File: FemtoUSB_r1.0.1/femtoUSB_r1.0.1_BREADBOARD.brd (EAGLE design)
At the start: 40.6 x 20.3 mm, 32 parts, among them IC1 ATSAMD21E18A-MUT

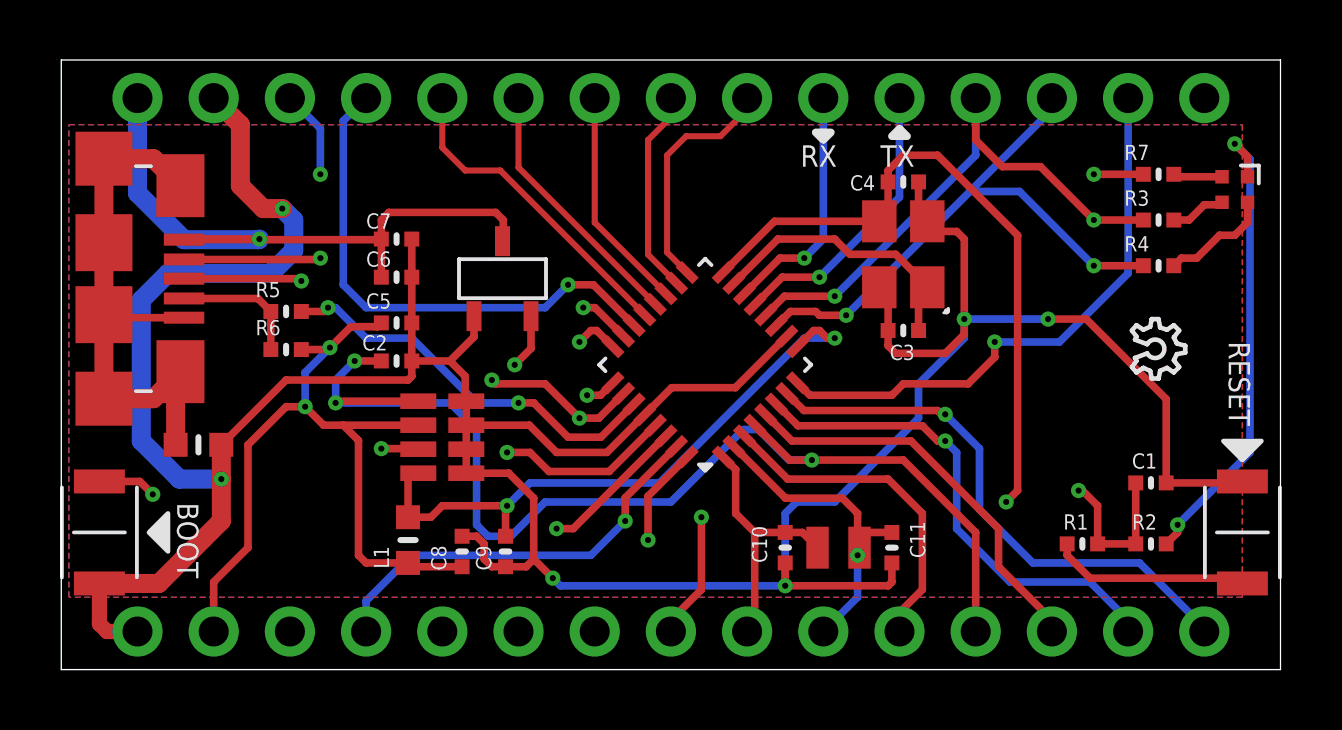
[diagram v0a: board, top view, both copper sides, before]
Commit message: Updating FemtoUSB r1.0.1 breadboard version
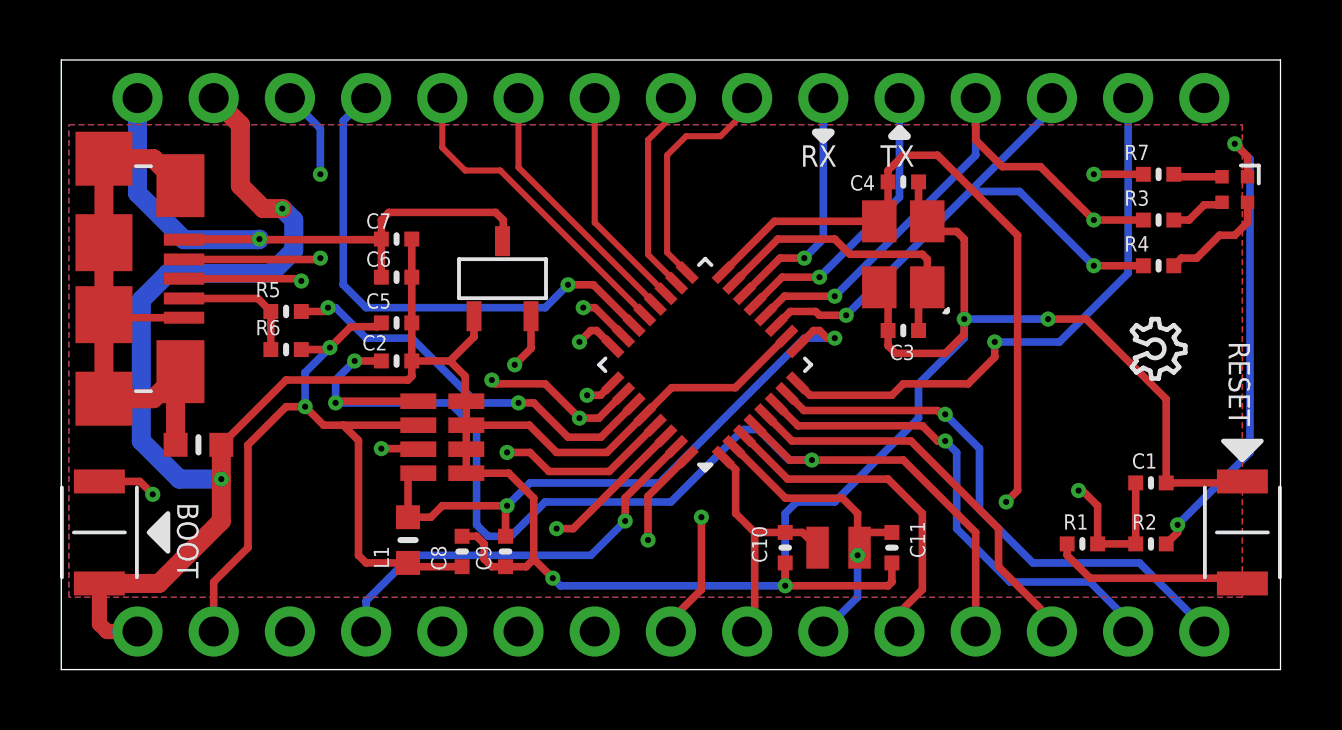
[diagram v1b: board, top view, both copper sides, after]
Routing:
- net PA14/XIN: track 9.36 -> 9.88 mm
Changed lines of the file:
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@@
 <contactref element="C3" pad="2"/>
 <wire x1="28.867" y1="12.743" x2="28.867" y2="12.789" width="0.254" layer="1"/>
-<wire x1="28.867" y1="12.789" x2="27.813" y2="13.843" width="0.254" layer="1"/>
 <wire x1="23.886234375" y1="14.351" x2="22.41759375" y2="12.882359375" width="0.254" layer="1"/>
-<wire x1="27.813" y1="13.843" x2="26.289" y2="13.843" width="0.254" layer="1"/>
+<wire x1="28.702" y1="13.843" x2="26.289" y2="13.843" width="0.254" layer="1"/>
 <wire x1="26.289" y1="13.843" x2="25.781" y2="14.351" width="0.254" layer="1"/>
 <wire x1="25.781" y1="14.351" x2="23.886234375" y2="14.351" width="0.254" layer="1"/>
 <wire x1="28.867" y1="12.789" x2="28.575" y2="12.497" width="0.254" layer="1"/>
 <wire x1="28.575" y1="12.497" x2="28.575" y2="11.303" width="0.254" layer="1"/>
+<wire x1="28.867" y1="12.789" x2="28.867" y2="13.678" width="0.254" layer="1"/>
+<wire x1="28.867" y1="13.678" x2="28.702" y2="13.843" width="0.254" layer="1"/>
 </signal>
 <signal name="PA15/XOUT">
